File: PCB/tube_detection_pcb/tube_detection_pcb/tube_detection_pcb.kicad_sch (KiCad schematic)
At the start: 12 parts, among them J1 B6B-XH-A, U1 DM3CQF1003L01, U2 DM3CQF1003L01, U3 DM3CQF1003L01, U4 DM3CQF1003L01, U5 DM3CQF1003L01, U6 SN74HC165N

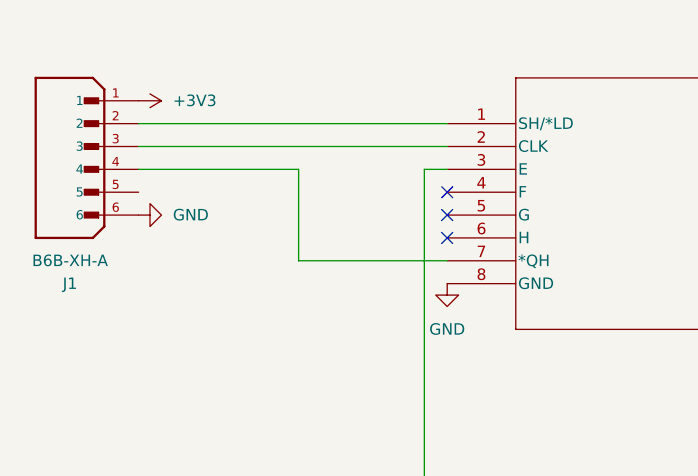
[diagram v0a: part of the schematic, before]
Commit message: changes to display and tube pcb
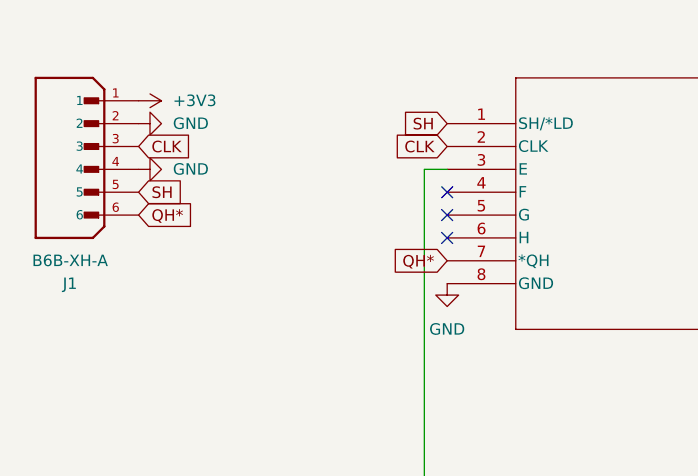
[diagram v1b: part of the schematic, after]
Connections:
- net GND: now also J1.2, J1.4; no longer J1.6
- net SH: now reaches U6.1 (SH/*LD)
- net SH: now also J1.5; no longer J1.2
- net CLK: now reaches J1.3, U6.2 (CLK)
- net QH*: now reaches U6.7 (*QH)
- net QH*: now also J1.6; no longer J1.4
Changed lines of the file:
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@@
-	(wire
-		(pts
-			(xy 36.83 50.8) (xy 71.12 50.8)
-		)
-		(stroke
-			(width 0)
-			(type default)
-		)
-	)
 	(wire
 		(pts
@@
 	(wire
 		(pts
-			(xy 36.83 55.88) (xy 54.61 55.88)
-		)
-		(stroke
-			(width 0)
-			(type default)
-		)
-	)
-	(wire
-		(pts
 			(xy 149.86 63.5) (xy 142.24 63.5)
 		)
@@
 	(wire
 		(pts
-			(xy 36.83 53.34) (xy 71.12 53.34)
-		)
-		(stroke
-			(width 0)
-			(type default)
-		)
-	)
-	(wire
-		(pts
-			(xy 54.61 66.04) (xy 71.12 66.04)
-		)
-		(stroke
-			(width 0)
-			(type default)
-		)
-	)
-	(wire
-		(pts
 			(xy 152.4 81.28) (xy 152.4 60.96)
 		)
@@
 	(wire
 		(pts
-			(xy 54.61 55.88) (xy 54.61 66.04)
-		)
-		(stroke
-			(width 0)
-			(type default)
-		)
-	)
-	(wire
-		(pts
 			(xy 149.86 93.98) (xy 149.86 63.5)
 		)
@@
 			(width 0)
 			(type default)
+		)
+	)
+	(global_label "CLK"
+		(shape input)
+		(at 36.83 53.34 0)
+		(fields_autoplaced yes)
+		(effects
+			(font
+				(size 1.27 1.27)
+			)
+			(justify left)
+		)
+		(property "Intersheetrefs" "${INTERSHEET_REFS}"
+			(at 43.3833 53.34 0)
+			(effects
+				(font
+					(size 1.27 1.27)
+				)
+				(justify left)
+				(hide yes)
+			)
+		)
+	)
+	(global_label "QH*"
+		(shape input)
+		(at 36.83 60.96 0)
+		(fields_autoplaced yes)
+		(effects
+			(font
+				(size 1.27 1.27)
+			)
+			(justify left)
+		)
+		(property "Intersheetrefs" "${INTERSHEET_REFS}"
+			(at 43.4438 60.96 0)
+			(effects
+				(font
+					(size 1.27 1.27)
+				)
+				(justify left)
+				(hide yes)
+			)
+		)
+	)
+	(global_label "SH"
+		(shape input)
+		(at 71.12 50.8 180)
+		(fields_autoplaced yes)
+		(effects
+			(font
+				(size 1.27 1.27)
+			)
+			(justify right)
+		)
+		(property "Intersheetrefs" "${INTERSHEET_REFS}"
+			(at 65.5948 50.8 0)
+			(effects
+				(font
+					(size 1.27 1.27)
+				)
+				(justify right)
+				(hide yes)
+			)
+		)
+	)
+	(global_label "SH"
+		(shape input)
+		(at 36.83 58.42 0)
+		(fields_autoplaced yes)
+		(effects
+			(font
+				(size 1.27 1.27)
+			)
+			(justify left)
+		)
+		(property "Intersheetrefs" "${INTERSHEET_REFS}"
+			(at 42.3552 58.42 0)
+			(effects
+				(font
+					(size 1.27 1.27)
+				)
+				(justify left)
+				(hide yes)
+			)
+		)
+	)
+	(global_label "QH*"
+		(shape input)
+		(at 71.12 66.04 180)
+		(fields_autoplaced yes)
+		(effects
+			(font
+				(size 1.27 1.27)
+			)
+			(justify right)
+		)
+		(property "Intersheetrefs" "${INTERSHEET_REFS}"
+			(at 64.5062 66.04 0)
+			(effects
+				(font
+					(size 1.27 1.27)
+				)
+				(justify right)
+				(hide yes)
+			)
+		)
+	)
+	(global_label "CLK"
+		(shape input)
+		(at 71.12 53.34 180)
+		(fields_autoplaced yes)
+		(effects
+			(font
+				(size 1.27 1.27)
+			)
+			(justify right)
+		)
+		(property "Intersheetrefs" "${INTERSHEET_REFS}"
+			(at 64.5667 53.34 0)
+			(effects
+				(font
+					(size 1.27 1.27)
+				)
+				(justify right)
+				(hide yes)
+			)
 		)
 	)
@@
 	)
 	(symbol
+		(lib_id "power:GND")
+		(at 36.83 50.8 90)
+		(unit 1)
+		(exclude_from_sim no)
+		(in_bom yes)
+		(on_board yes)
+		(dnp no)
+		(fields_autoplaced yes)
+		(property "Reference" "#PWR015"
+			(at 43.18 50.8 0)
+			(effects
+				(font
+					(size 1.27 1.27)
+				)
+				(hide yes)
+			)
+		)
+		(property "Value" "GND"
+			(at 40.64 50.7999 90)
+			(effects
+				(font
+					(size 1.27 1.27)
+				)
+				(justify right)
+			)
+		)
+		(property "Footprint" ""
+			(at 36.83 50.8 0)
+			(effects
+				(font
+					(size 1.27 1.27)
+				)
+				(hide yes)
+			)
+		)
+		(property "Datasheet" ""
+			(at 36.83 50.8 0)
+			(effects
+				(font
+					(size 1.27 1.27)
+				)
+				(hide yes)
+			)
+		)
+		(property "Description" "Power symbol creates a global label with name \"GND\" , ground"
+			(at 36.83 50.8 0)
+			(effects
+				(font
+					(size 1.27 1.27)
+				)
+				(hide yes)
+			)
+		)
+		(pin "1"
+		)
+		(instances
+			(project "tube_detection_pcb"
+				(path "/8963d266-a6bd-42d9-bfbb-c9f3c747bccc"
+					(reference "#PWR015")
+					(unit 1)
+				)
+			)
+		)
+	)
+	(symbol
 		(lib_id "10k-resistor:MFP-25BRD52-10K")
 		(at 167.64 104.14 0)
@@
 	(symbol
 		(lib_id "power:GND")
-		(at 36.83 60.96 90)
+		(at 36.83 55.88 90)
 		(unit 1)
 		(exclude_from_sim no)
@@
 		(fields_autoplaced yes)
 		(property "Reference" "#PWR011"
-			(at 43.18 60.96 0)
+			(at 43.18 55.88 0)
 			(effects
 				(font
@@
 		)
 		(property "Value" "GND"
-			(at 40.64 60.9599 90)
+			(at 40.64 55.8799 90)
 			(effects
 				(font
@@
 		)
 		(property "Footprint" ""
-			(at 36.83 60.96 0)
+			(at 36.83 55.88 0)
 			(effects
 				(font
@@
 		)
 		(property "Datasheet" ""
-			(at 36.83 60.96 0)
+			(at 36.83 55.88 0)
 			(effects
 				(font
@@
 		)
 		(property "Description" "Power symbol creates a global label with name \"GND\" , ground"
-			(at 36.83 60.96 0)
-			(effects
-				(font
+			(at 36.83 55.88 0)
+			(effects
+				(font

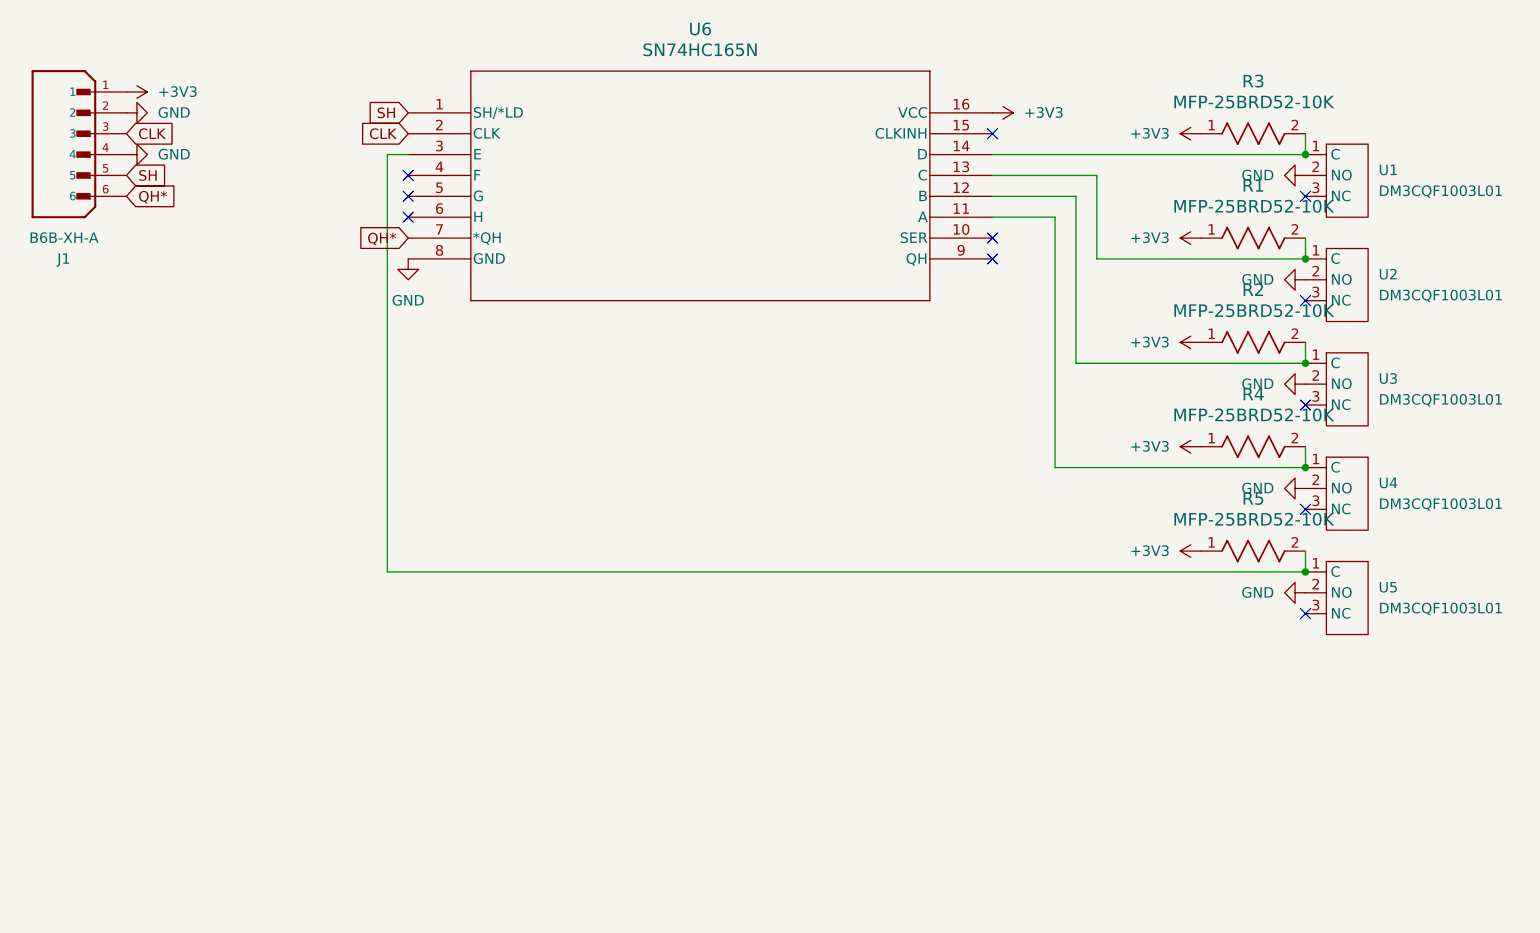
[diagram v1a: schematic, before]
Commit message: pcb silkscreens mostly
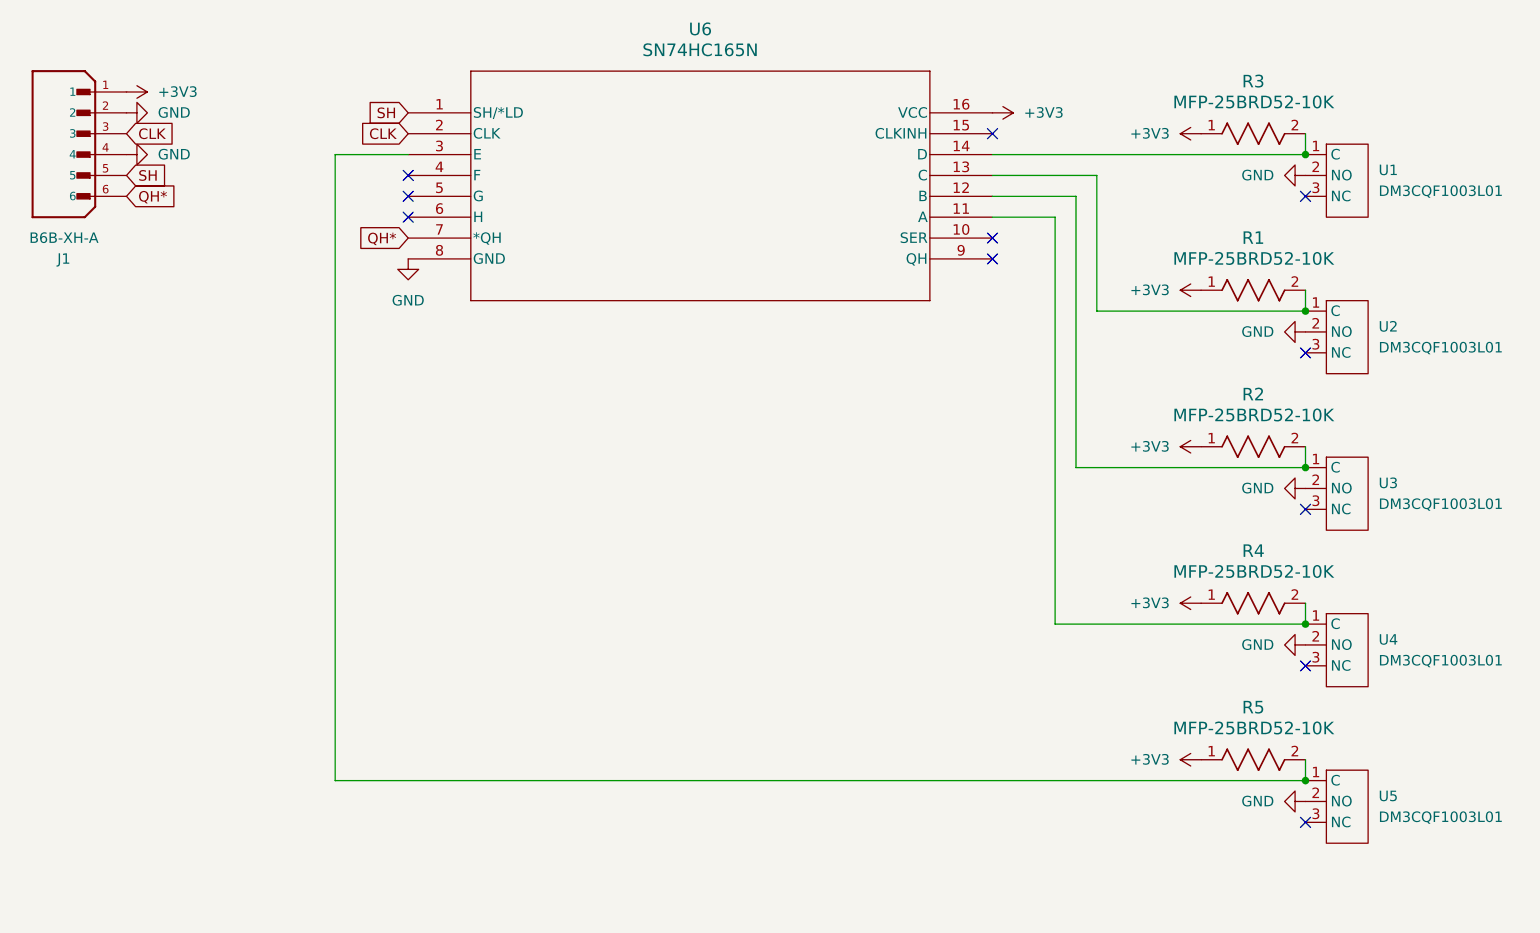
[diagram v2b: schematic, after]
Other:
- moved on the sheet: R1, R2, R4, R5, U2, U3, U4, U5

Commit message: pcb repin
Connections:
- net CLK: now also J1.5; no longer J1.3
- net GND: now also U6.10 (SER), U6.15 (CLKINH), U6.4 (F), U6.5 (G), U6.6 (H)
- net SH: now also J1.3; no longer J1.5
- no-connect marks 11 -> 6

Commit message: PCB updates
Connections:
- net CLK: now also J1.4; no longer J1.5
- net GND: now also U1.3 (NC), U2.3 (NC), U3.3 (NC), U4.3 (NC), U5.3 (NC); no longer J1.4, U1.2 (NO), U2.2 (NO), U3.2 (NO), U4.2 (NO), U5.2 (NO), U6.15 (CLKINH)
- net at R1.2, U2.1 (C): no longer U6.13 (C)
- net at R5.2, U5.1 (C): no longer U6.3 (E)
- net at R3.2, U1.1 (C): no longer U6.14 (D)
- net at R4.2, U4.1 (C): no longer U6.11 (A)
- net at R2.2, U3.1 (C): no longer U6.12 (B)
- new net: U3.2 (NO), U6.12 (B)
- new net: U5.2 (NO), U6.3 (E)
- new net: U1.2 (NO), U6.14 (D)
- new net: U4.2 (NO), U6.11 (A)
- new net: U2.2 (NO), U6.13 (C)
- new net CSn: J1.5, U6.15 (CLKINH)
- no-connect marks 6 -> 1
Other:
- moved on the sheet: R3, U1

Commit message: pcb finishing touches
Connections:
- net CSn: now also J1.6; no longer J1.5
- net QH*: now also J1.3; no longer J1.6
- net SH: now also J1.5; no longer J1.3
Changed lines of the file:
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@@
 	(global_label "QH*"
 		(shape input)
-		(at 36.83 60.96 0)
+		(at 36.83 53.34 0)
 		(fields_autoplaced yes)
 		(effects
@@
 		)
 		(property "Intersheetrefs" "${INTERSHEET_REFS}"
-			(at 43.4438 60.96 0)
+			(at 43.4438 53.34 0)
 			(effects
 				(font
@@
 	(global_label "SH"
 		(shape input)
-		(at 36.83 53.34 0)
+		(at 36.83 58.42 0)
 		(fields_autoplaced yes)
 		(effects
@@
 		)
 		(property "Intersheetrefs" "${INTERSHEET_REFS}"
-			(at 42.3552 53.34 0)
+			(at 42.3552 58.42 0)
 			(effects
 				(font
@@
 	(global_label "CSn"
 		(shape input)
-		(at 36.83 58.42 0)
+		(at 36.83 60.96 0)
 		(fields_autoplaced yes)
 		(effects
@@
 		)
 		(property "Intersheetrefs" "${INTERSHEET_REFS}"
-			(at 43.4437 58.42 0)
+			(at 43.4437 60.96 0)
 			(effects
 				(font
